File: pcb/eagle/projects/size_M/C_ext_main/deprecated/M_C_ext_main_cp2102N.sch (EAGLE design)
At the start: 20 parts

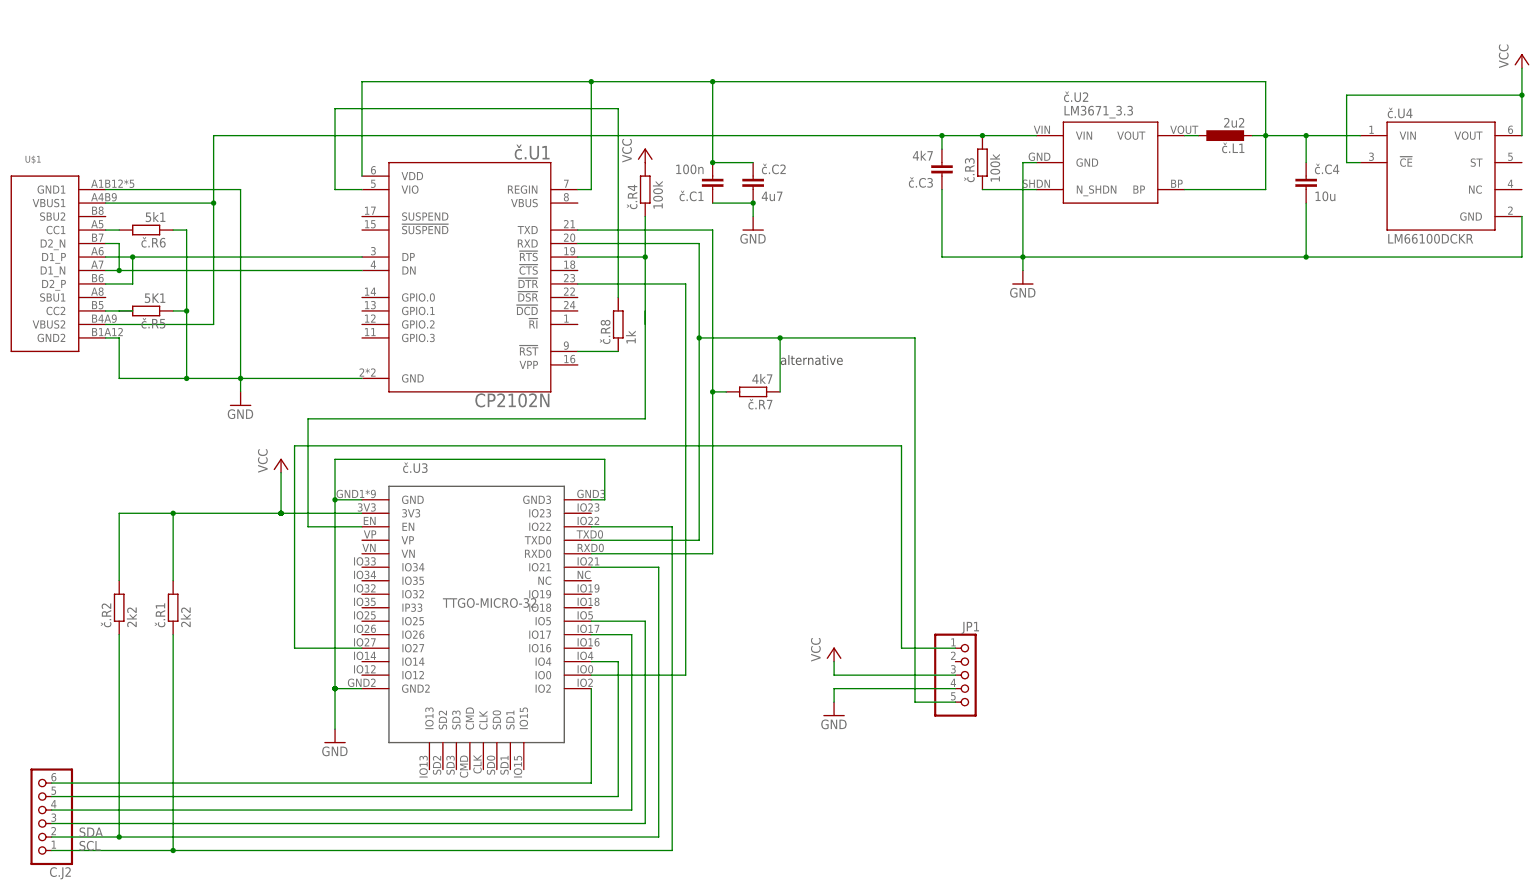
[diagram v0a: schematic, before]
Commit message: version 8 main changes * ideal diode separated 3v3 DC-DC to protect it from back current * smaller package of ina 219 * usage of tssop attiny v2 in adapter * and change of PA5 to PB2 with ^ and ~ (originally used for shield power switch - now PB3) * step motor shield * out signal for BT module
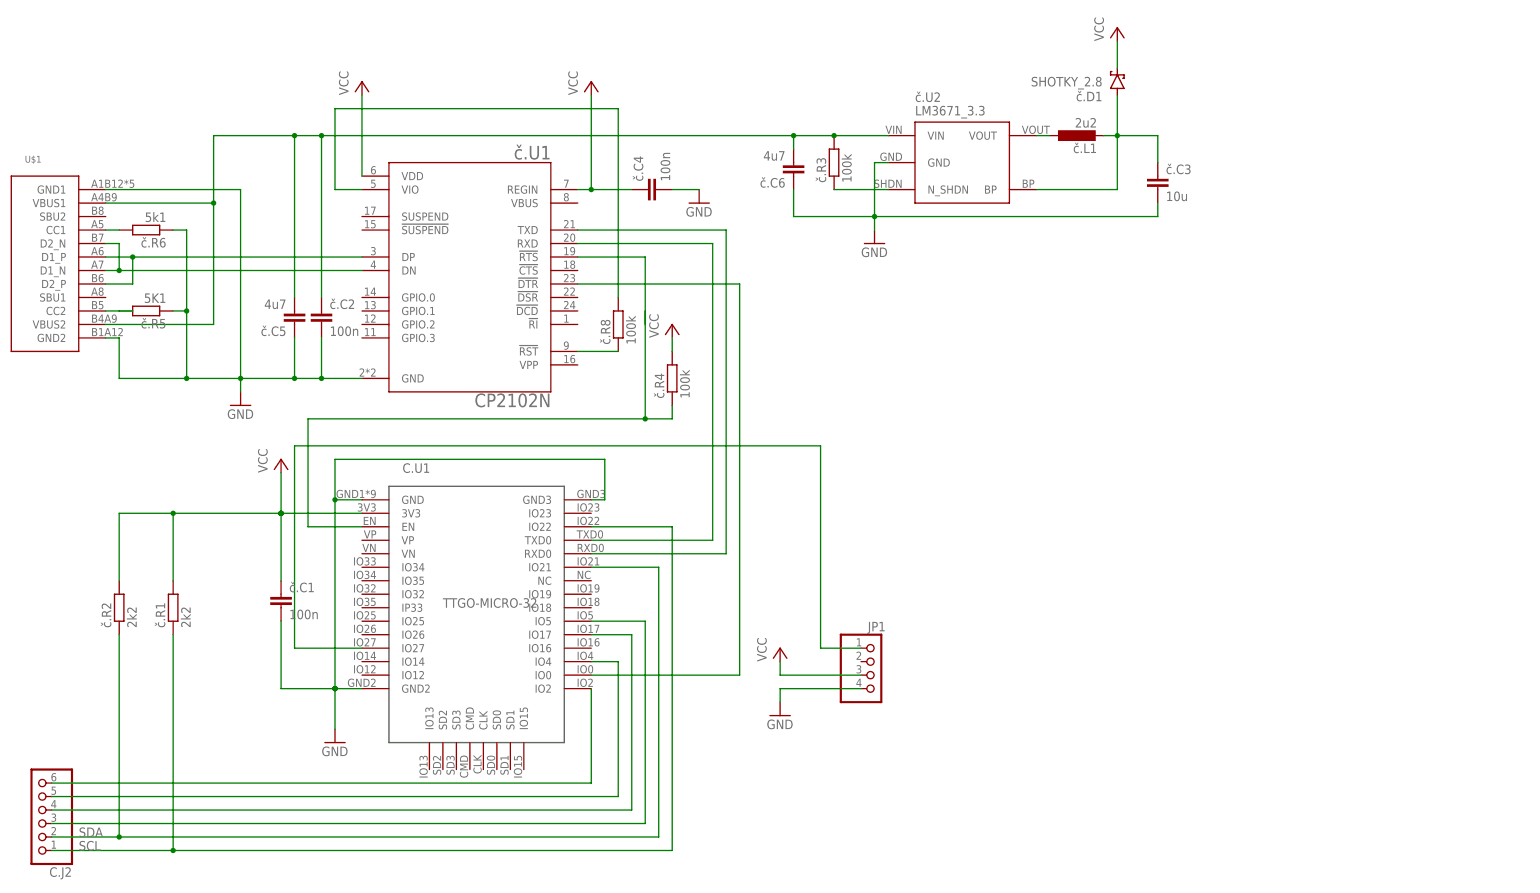
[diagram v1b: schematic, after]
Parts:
- removed č.R7: 4k7, rcl:R-EU_R0603
- removed č.U4: LM66100DCKR, LM66100DCKR:LM66100DCKR
- added č.C5, č.C6: 4u7, rcl:C-EUC0603
- added č.D1: SHOTKY_2.8, hugo:SHOTKY_2.8
- JP1: device pinhead2:PINHD-1X5 -> pinhead2:PINHD-1X4
- č.C2: value 4u7 -> 100n
- č.C3: value 4k7 -> 10u; device rcl:C-EUC0603 -> rcl:C-EUC0805
- č.C4: value 10u -> 100n
- č.R8: value 1k -> 100k
- renumbered č.U3 to C.U1
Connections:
- removed net VCC1: č.C1.2, č.C2.1, č.C4.1, č.L1.2, č.U1.REGIN, č.U1.VDD, č.U2.BP, č.U4.VIN
- new net N$5: č.C3.1, č.D1.A, č.L1.2, č.U2.BP
- net GND: now also č.C1.2, č.C3.2, č.C5.1, č.C6.1; no longer č.C1.1, č.C3.1, č.U4.GND
- net RX: no longer JP1.5, č.R7.1
- net TX: no longer č.R7.2
- net VCC: now also č.C1.1, č.C4.1, č.D1.C, č.U1.REGIN, č.U1.VDD; no longer č.U4.!CE, č.U4.VOUT
- net VUSB: now also č.C2.1, č.C5.2, č.C6.2; no longer č.C3.2
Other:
- note removed: "alternative"
- moved on the sheet: č.C1, č.C2, č.C3, č.C4, č.L1, č.R3, č.R4, č.U2
